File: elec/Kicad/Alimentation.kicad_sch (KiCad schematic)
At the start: 16 parts

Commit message: did some change (but i have to verify them)
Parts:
- added J?: USB_B_Micro_MAIN, symbol Connector:USB_B_Micro
- added Q?: MMS9013HE3, Package_TO_SOT_SMD:SOT-23, symbol Transistor_BJT:2N3055
- added R?: 100, symbol Device:R
- added R? (x2): 0, symbol Device:R
- added R?: 10K, symbol Device:R
- added R?: 100K, symbol Device:R
- added R?: 1.5K, symbol Device:R
- added R?: 36K, symbol Device:R
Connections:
- net GND: now also J?.5 (GND), J?.6 (Shield), R?.1, R?.2
- new net: J?.2 (D-), R?.1
- new net: J?.3 (D+), R?.1, R?.1
- new net: J?.4 (ID), R?.1
- new net: Q?.1 (B), R?.1, R?.1, R?.2
- new net: Q?.2 (E), R?.2
- new net 3V3_ST_LINK: Q?.3 (C)
- new net 5V_USB_ST_LINK: J?.1 (VBUS), R?.2
- new net USB_DM: R?.2
- new net USB_DP: R?.2
- new net USB_RENUMn: R?.2

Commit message: boot/reset button
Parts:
- removed L?: Ferrite (10uH), symbol Device:L
- removed V1: Vin (5-3.5)V, symbol Device:Battery
- added C?: 1uF, symbol Device:C
- added C?: 1u, symbol Device:C
- added C?: 100nF, symbol Device:C
- added D1: GREEN, symbol Device:LED
- added FB?: 100R, symbol Device:FerriteBead
- added J?: USB_B_Micro_MAIN, symbol Connector:USB_B_Micro
- added L?: 27n, symbol Device:L
- added R?: 1K5, symbol Device:R
- J?: value USB_B_Micro_MAIN -> USB_B_Micro_COPY
- R?: value 1.5K -> 1K5
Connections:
- net VDD is gone; now on net +3V3: C?.1, C?.1, C?.1, C?.1
- net VDDA is gone; now on net +3V3: C?.1, C?.1
- net +3V3: now also TP1.1, D1.2 (A), L?.1
- net GND: now also C?.2, C?.2, C?.2, J?.5 (GND)
- net at C?.2, R?.2, U?.2 (PG): now also R?.2
- net VCC: now reaches C?.1, U?.1 (EN), U?.7 (VIN)
- net VCC: now also C?.1, FB?.2
- new net: D1.1 (K), R?.1
- new net +3.3VA: C?.1, C?.1, L?.2
- new net +5V: FB?.1, J?.1 (VBUS)
- new net USB_D+: J?.3 (D+)
- new net USB_D-: J?.2 (D-)
- no-connect marks 0 -> 3
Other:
- note added: "Copie de la schématique STM32L0538-DISCO"
- note added: "passe bas pour filtrer VDDA"
- moved on the sheet: C?, J?, Q?, R?, TP1

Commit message: merci Linux
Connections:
- net VCC renamed Vin
- no-connect marks 3 -> 2
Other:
- note added: "Est-ce qu'on ground le shield (Phil ne l'a pas faite, mais je pense que ce serait mieux de le faire)"
- note added: "In Phil we Trust"
- note added: "La valeur de la res pour la DEL est haute(1K5), mais normal selon Phil's Lab"
- note added: "NEAR MCU"
- moved on the sheet: C?, L?

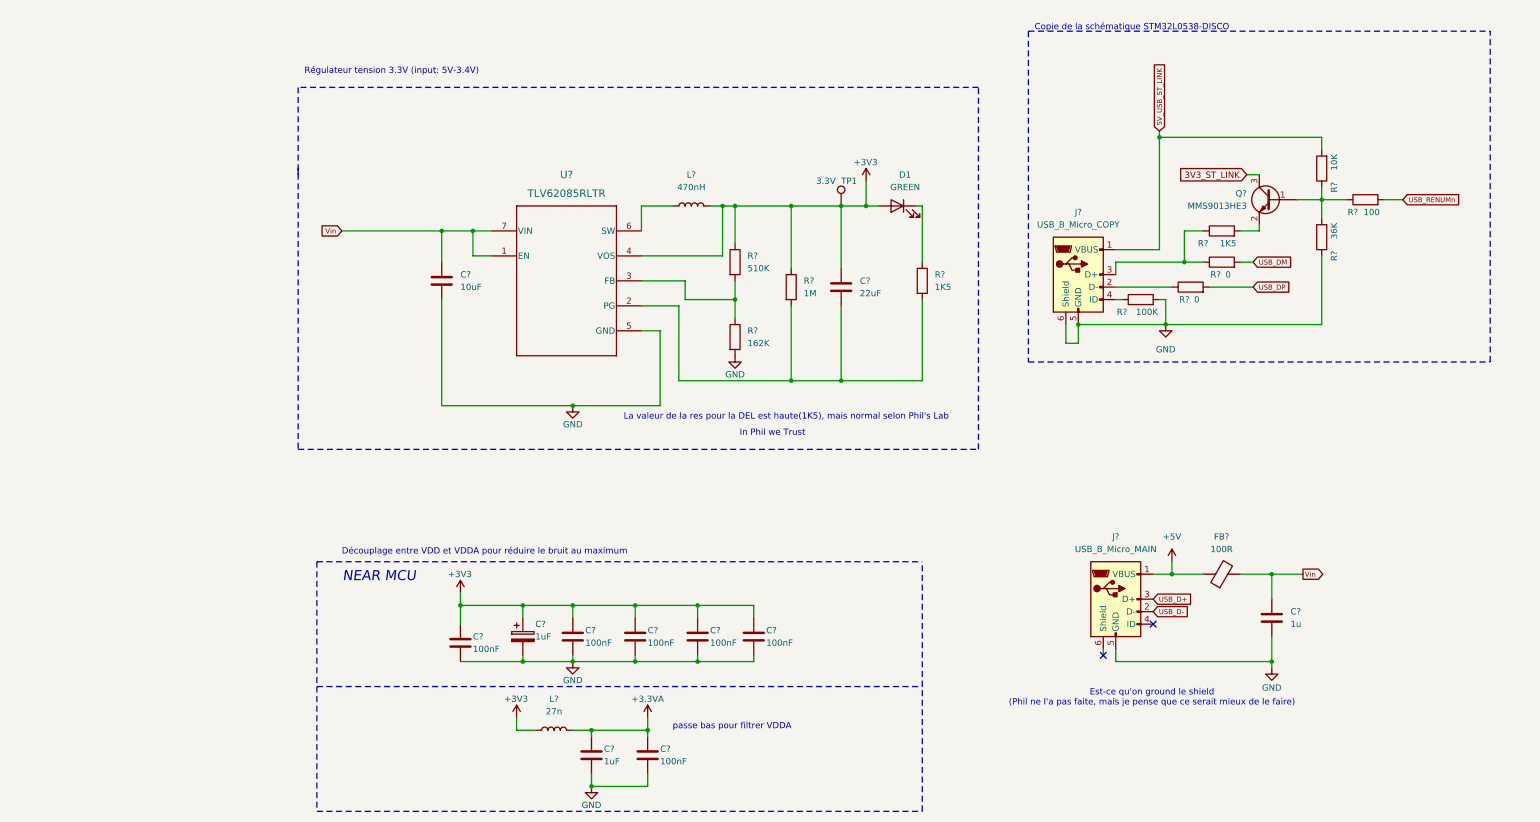
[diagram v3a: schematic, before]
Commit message: start the battery managemennt
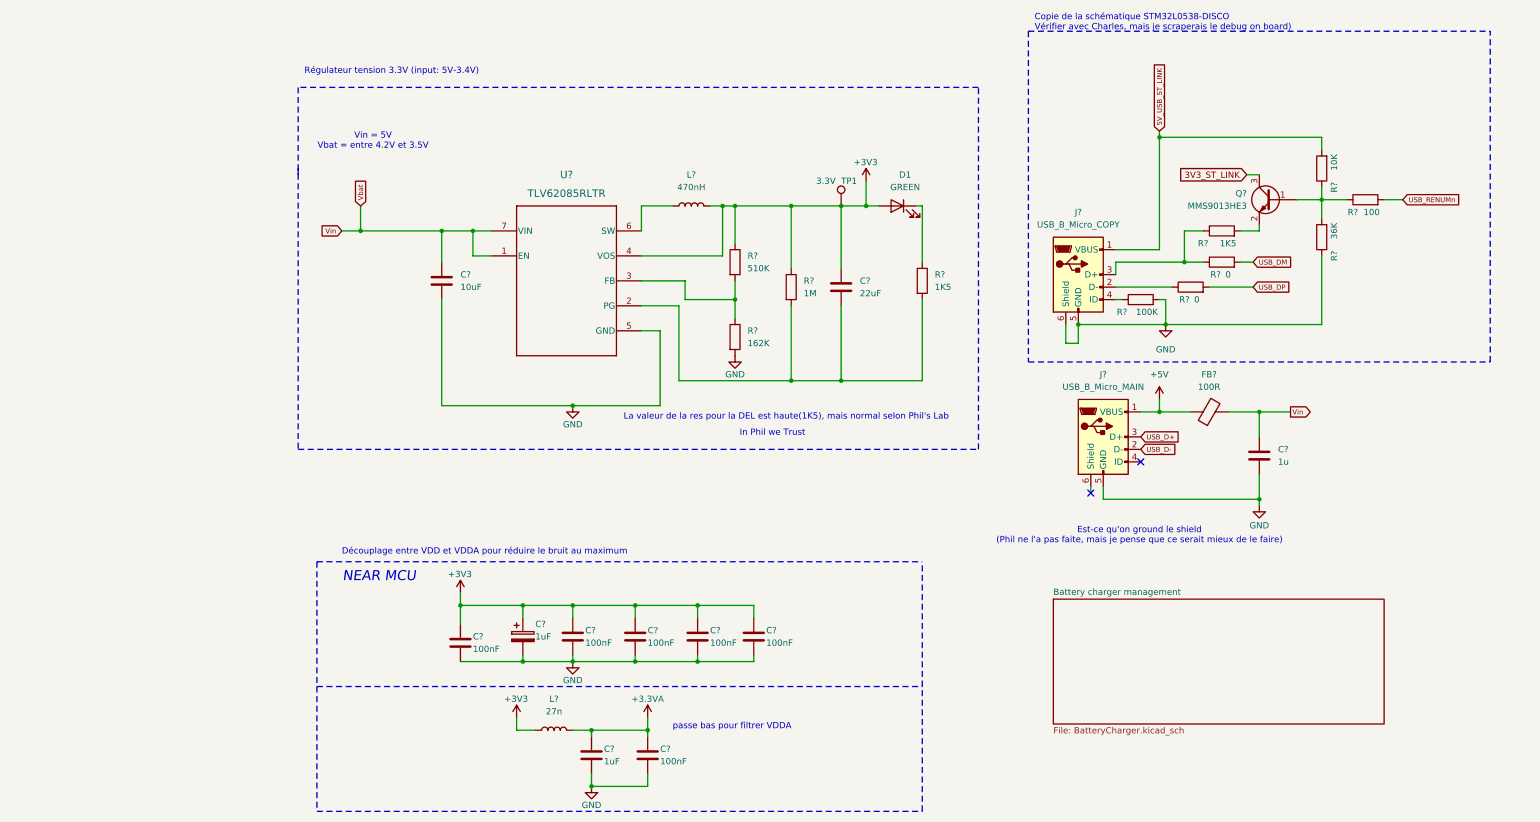
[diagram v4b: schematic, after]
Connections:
- net Vin renamed Vbat
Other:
- added sheet Battery charger management (BatteryCharger.kicad_sch)
- note added: "Copie de la schématique STM32L0538-DISCO Vérifier avec Charles, mais je scraperais le debug on board)"
- note added: "Vin = 5V Vbat = entre 4.2V et 3.5V"
- note removed: "Copie de la schématique STM32L0538-DISCO"
- moved on the sheet: C?, FB?, J?

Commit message: Presque finin la la gestion de la batterie (faire les dels demains)
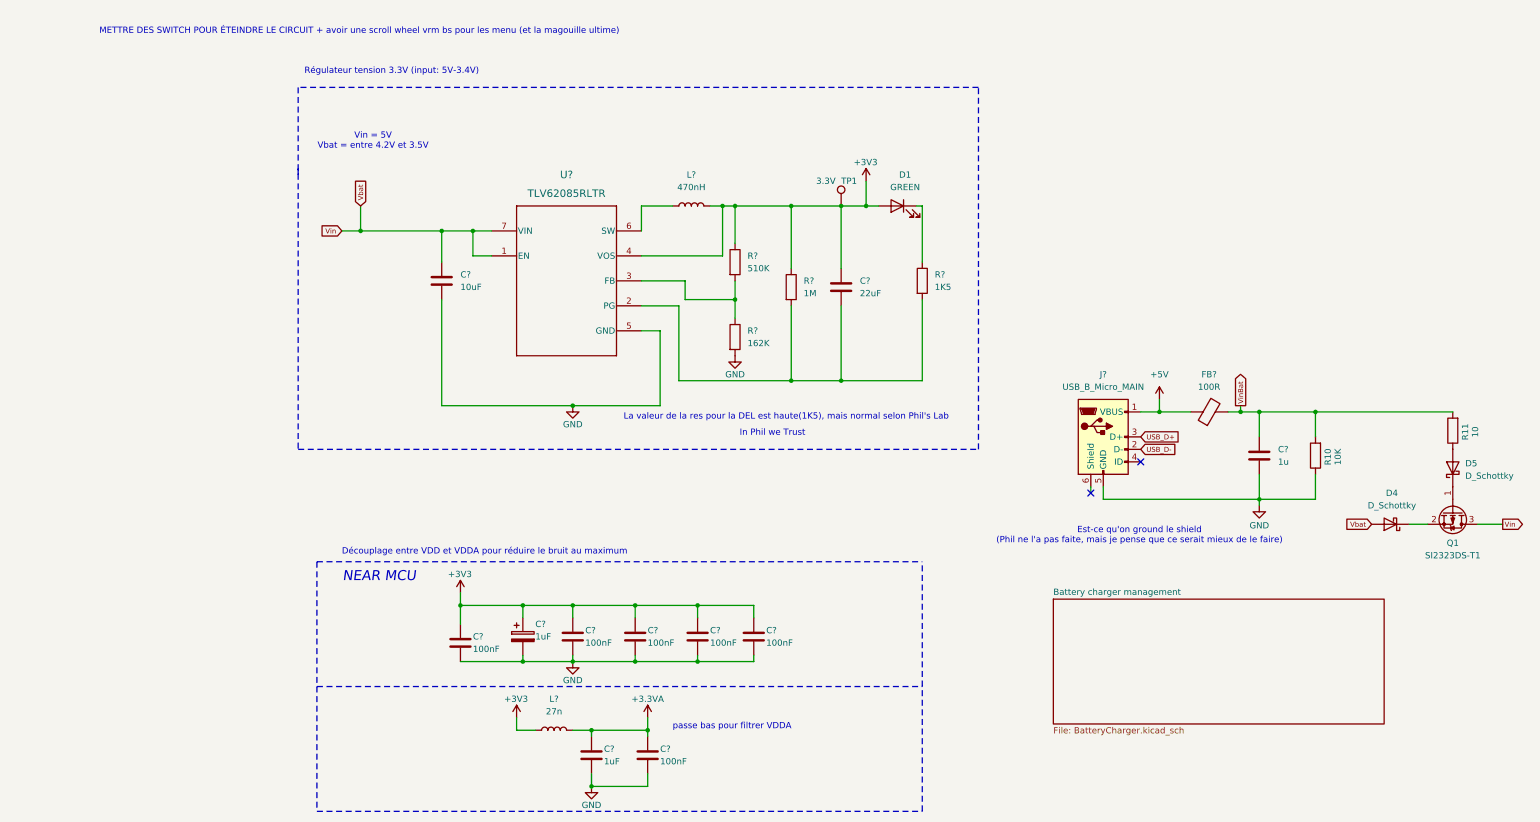
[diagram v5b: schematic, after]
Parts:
- removed J?: USB_B_Micro_COPY, symbol Connector:USB_B_Micro
- removed Q?: MMS9013HE3, Package_TO_SOT_SMD:SOT-23, symbol Transistor_BJT:2N3055
- removed R?: 100, symbol Device:R
- removed R? (x2): 0, symbol Device:R
- removed R?: 10K, symbol Device:R
- removed R?: 100K, symbol Device:R
- removed R?: 1K5, symbol Device:R
- removed R?: 36K, symbol Device:R
- added D4, D5: D_Schottky, symbol Device:D_Schottky
- added Q1: SI2323DS-T1, Package_TO_SOT_SMD:SOT-23, symbol Transistor_FET:AO3401A
- added R10: 10K, symbol Device:R
- added R11: 10, symbol Device:R
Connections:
- net GND: now also R10.1
- net Vbat: now also D4.2 (A), Q1.3 (D); no longer C?.1, FB?.2
- new net: D5.2 (A), R11.1
- new net: D4.1 (K), Q1.2 (S)
- new net: D5.1 (K), Q1.1 (G)
- new net VinBat: C?.1, FB?.2, R10.2, R11.2
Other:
- note added: "METTRE DES SWITCH POUR ÉTEINDRE LE CIRCUIT + avoir une scroll wheel vrm bs pour les menu (et la magouille ultime)"
- note removed: "Copie de la schématique STM32L0538-DISCO Vérifier avec Charles, mais je scraperais le debug on board)"

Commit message: sa progresse. Battery management fini + humidity/temp sensor + bouton
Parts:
- removed D4, D5: D_Schottky, symbol Device:D_Schottky
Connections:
- net Vbat: now also Q1.2 (S)
- net at R11.1: now also Q1.1 (G)
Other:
- note added: "LED QUI INDIQUE QUE LE CIRCUIT EST ALIMENTÉ"
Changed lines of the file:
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@@
+	(wire
+		(pts
+			(xy 266.7 102.87) (xy 266.7 110.49)
+		)
+		(stroke
+			(width 0)
+			(type default)
+		)
+	)
 	(wire
 		(pts
@@
 	(wire
 		(pts
-			(xy 257.81 118.11) (xy 261.62 118.11)
-		)
-		(stroke
-			(width 0)
-			(type default)
-		)
-	)
-	(wire
-		(pts
 			(xy 60.96 58.42) (xy 60.96 64.77)
 		)
@@
 		(pts
 			(xy 60.96 93.98) (xy 87.63 93.98)
+		)
+		(stroke
+			(width 0)
+			(type default)
+		)
+	)
+	(wire
+		(pts
+			(xy 250.19 118.11) (xy 261.62 118.11)
 		)
 		(stroke
@@
 	(text "METTRE DES SWITCH POUR ÉTEINDRE LE CIRCUIT + avoir une scroll wheel vrm bs pour les menu (et la magouille ultime)"
 		(exclude_from_sim no)
-		(at 44.196 17.78 0)
+		(at 74.676 17.78 0)
+		(effects
+			(font
+				(size 1.27 1.27)
+			)
+		)
+	)
+	(text "LED QUI INDIQUE QUE LE CIRCUIT EST ALIMENTÉ"
+		(exclude_from_sim no)
+		(at 145.542 39.116 0)
 		(effects
 			(font
@@
 	)
 	(symbol
-		(lib_id "Device:D_Schottky")
-		(at 254 118.11 180)
-		(unit 1)
-		(exclude_from_sim no)
-		(in_bom yes)
-		(on_board yes)
-		(dnp no)
-		(fields_autoplaced yes)
-		(property "Reference" "D4"
-			(at 254.3175 111.76 0)
-			(effects
-				(font
-					(size 1.27 1.27)
-				)
-			)
-		)
-		(property "Value" "D_Schottky"
-			(at 254.3175 114.3 0)
-			(effects
-				(font
-					(size 1.27 1.27)
-				)
-			)
-		)
-		(property "Footprint" ""
-			(at 254 118.11 0)
-			(effects
-				(font
-					(size 1.27 1.27)
-				)
-				(hide yes)
-			)
-		)
-		(property "Datasheet" "~"
-			(at 254 118.11 0)
-			(effects
-				(font
-					(size 1.27 1.27)
-				)
-				(hide yes)
-			)
-		)
-		(property "Description" "Schottky diode"
-			(at 254 118.11 0)
-			(effects
-				(font
-					(size 1.27 1.27)
-				)
-				(hide yes)
-			)
-		)
-		(pin "1"
-		)
-		(pin "2"
-		)
-		(instances
-			(project ""
-				(path "/a1545928-1195-40b9-b3c4-78f837012afb/47f0fc71-ff78-496f-bb04-036a9aeaa71c/6f59428e-8e72-4854-8d86-784df1ffb46d"
-					(reference "D4")
-					(unit 1)
-				)
-			)
-		)
-	)
-	(symbol
 		(lib_id "power:GND")
 		(at 120.65 83.82 0)
@@
 					(unit 1)
 				)
-			)
-		)
-	)
-	(symbol
-		(lib_id "Device:D_Schottky")
-		(at 266.7 106.68 90)
-		(unit 1)
-		(exclude_from_sim no)
-		(in_bom yes)
-		(on_board yes)
-		(dnp no)
-		(fields_autoplaced yes)
-		(property "Reference" "D5"
-			(at 269.24 105.7274 90)
-			(effects
-				(font
-					(size 1.27 1.27)
-				)
-				(justify right)
-			)
-		)
-		(property "Value" "D_Schottky"
-			(at 269.24 108.2674 90)
-			(effects
-				(font
-					(size 1.27 1.27)
-				)
-				(justify right)
-			)
-		)
-		(property "Footprint" ""
-			(at 266.7 106.68 0)
-			(effects
-				(font
-					(size 1.27 1.27)
-				)
-				(hide yes)
-			)
-		)
-		(property "Datasheet" "~"
-			(at 266.7 106.68 0)
-			(effects
-				(font
-					(size 1.27 1.27)
-				)
-				(hide yes)
-			)
-		)
-		(property "Description" "Schottky diode"
-			(at 266.7 106.68 0)
-			(effects
-				(font
-					(size 1.27 1.27)
-				)
-				(hide yes)
-			)
-		)
-		(pin "1"
-		)
-		(pin "2"
-		)
-		(instances
-			(project "rulerSchematic"
-				(path "/a1545928-1195-40b9-b3c4-78f837012afb/47f0fc71-ff78-496f-bb04-036a9aeaa71c/6f59428e-8e72-4854-8d86-784df1ffb46d"
-					(reference "D5")
-					(unit 1)
-				)

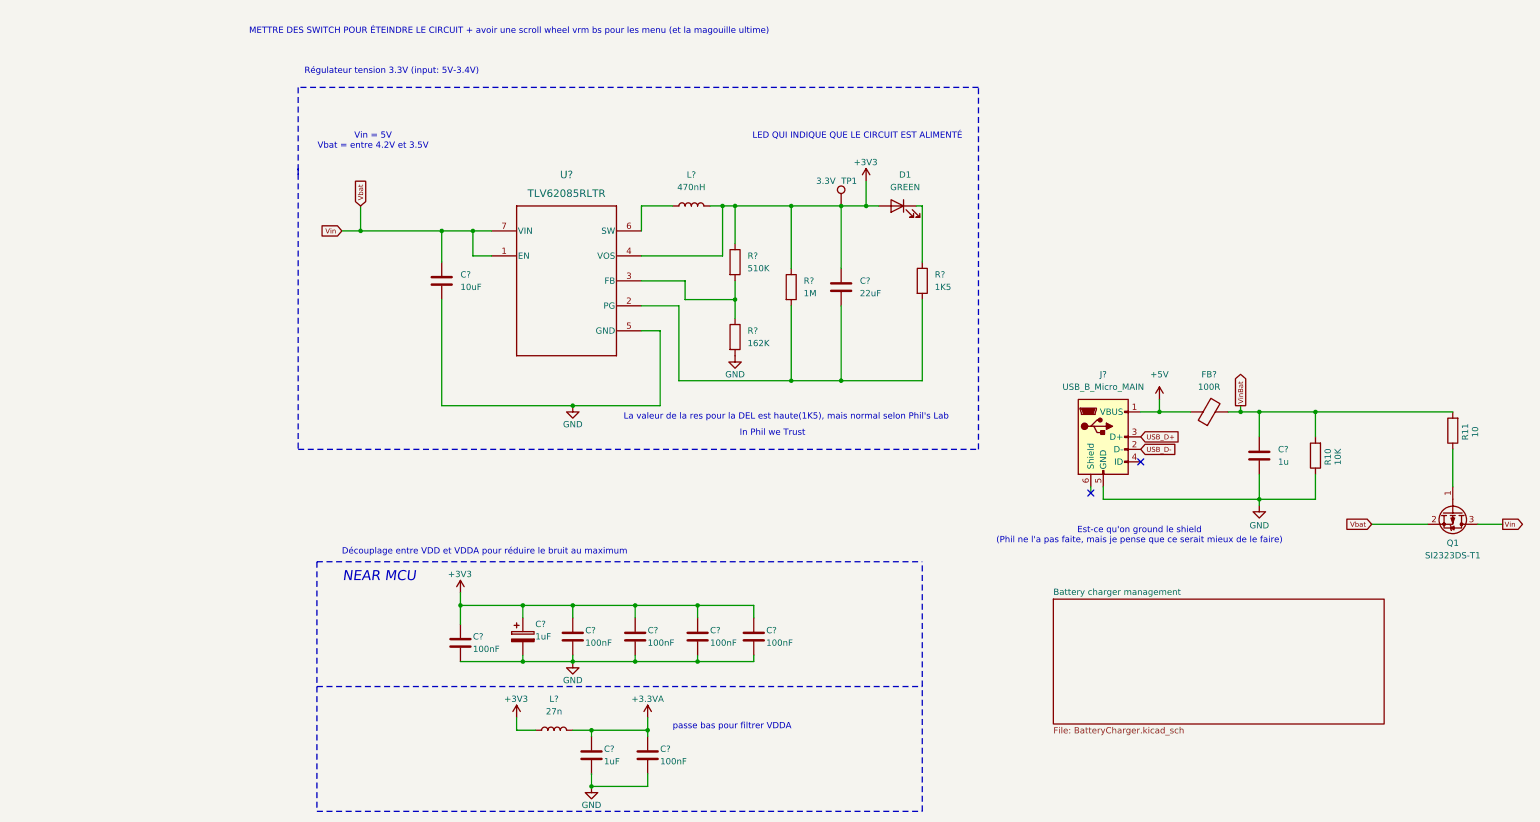
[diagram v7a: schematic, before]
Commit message: push pour charles (début de l'ajout diviseur tension pour la batterie)
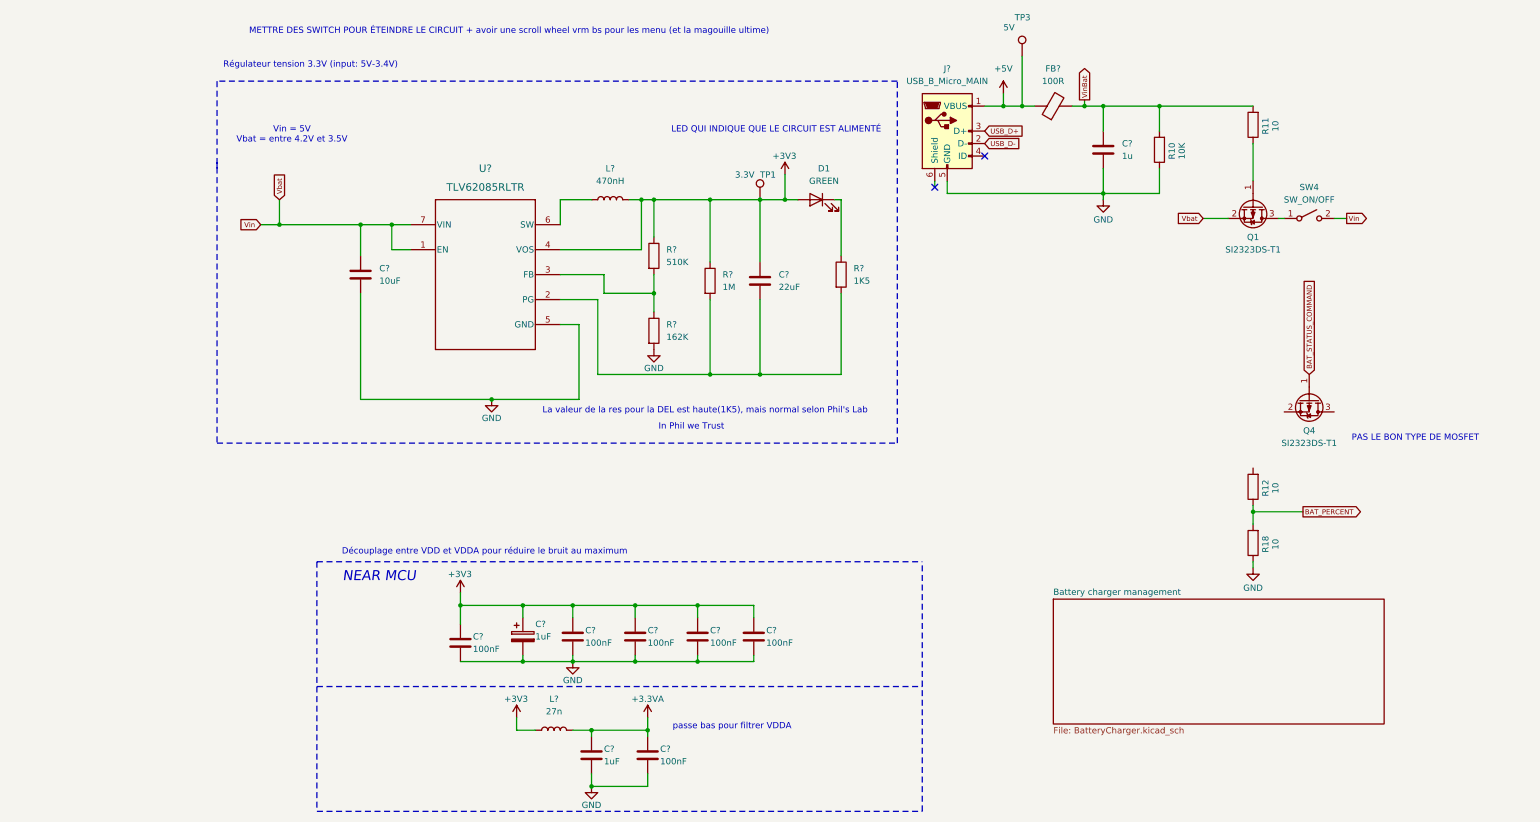
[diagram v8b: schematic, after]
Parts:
- added Q4: SI2323DS-T1, Package_TO_SOT_SMD:SOT-23, symbol Transistor_FET:AO3401A
- added R12, R18: 10, symbol Device:R
- added SW4: SW_ON/OFF, symbol Switch:SW_SPST
- added TP3: 5V, symbol Connector:TestPoint
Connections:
- net +5V: now also TP3.1
- net GND: now also R18.1
- net Vbat: now also SW4.2 (B); no longer Q1.3 (D)
- new net: Q1.3 (D), SW4.1 (A)
- new net BAT_PERCENT: R12.1, R18.2
- new net BAT_STATUS_COMMAND: Q4.1 (G)
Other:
- note added: "PAS LE BON TYPE DE MOSFET"
- note removed: "Est-ce qu'on ground le shield (Phil ne l'a pas faite, mais je pense que ce serait mieux de le faire)"
- moved on the sheet: C?, D1, FB?, J?, L?, Q1, R10, R11, R?, TP1, U?
